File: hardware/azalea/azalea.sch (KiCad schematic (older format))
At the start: 7 parts

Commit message: azalea: completed most of schematic apart from the expansion interface
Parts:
- removed J?: GSG-USB-MICRO-B-SHIELDED, symbol GSG-USB-MICRO-B-SHIELDED
- added C? (x2): 18pF, symbol C
- added C? (x2): 47pF, symbol C
- added C?: 10uF, symbol C
- added C?: 1uF, symbol C
- added C? (x15): 100nF, symbol C
- added D? (x4): LED, symbol LED
- added FB?: FILTER, symbol FILTER
- added J2: GSG-USB-MICRO-B-SHIELDED, symbol GSG-USB-MICRO-B-SHIELDED
- added P?: JTAG, symbol CONN_02X05
- added P?: DBGEN, symbol CONN_01X01
- added P?: TRST, symbol CONN_01X01
- added R? (x12): 10k, symbol R
- added R? (x2): 12.0k, symbol R
- added R? (x2): 33.0, symbol R
- added R? (x4): 330, symbol R
- added SW?: RESET, symbol SW_PUSH
- added SW?: DFU, symbol SW_PUSH
- J1: renamed from J?; Description (none) -> CONN RCPT REV MICRO USB TYPE B; Manufacturer (none) -> FCI; Part Number (none) -> 10103592-0001LF
- U1: renamed from U?; Description (none) -> IC MCU ARM ROMLESS 144LQFP; Manufacturer (none) -> NXP; Part Number (none) -> LPC4330FBD144,551
- U?: Description (none) -> IC REG LDO 3.3V .3A SOT23; Manufacturer (none) -> Diodes Inc.; Part Number (none) -> AP7333-33SAG-7
- U?: Description (none) -> IC USB DUAL ESD PROTECT 6TSOP; Manufacturer (none) -> NXP; Part Number (none) -> IP4220CZ6,125
- U?: value W25Q80BV -> W25Q16DV; Description (none) -> IC FLASH 16MBIT 104MHZ 8SOIC; Manufacturer (none) -> Winbond; Part Number (none) -> W25Q16DVSSIG
- X?: Description (none) -> CRYSTAL 12.000 MHZ 12PF SMD; Manufacturer (none) -> TXC; Part Number (none) -> 7V-12.000MAAE-T
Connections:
- net at U?.1 (IN): now also U1.21 (USB0_VBUS), C?.1, FB?.2
- net VCC: now reaches U?.2 (OUT)
- net VCC: now also U1.107 (VDDIO), U1.111 (VDDIO), U1.131 (VDDREG), U1.141 (VDDIO), U1.16 (USB0_VDDA3V3_DRIVER), U1.17 (USB0_VDDA3V3), U1.25 (VDDREG), U1.36 (VDDIO), U1.41 (VDDIO), U1.5 (VDDIO), U1.59 (VDDREG), U1.71 (VDDIO), U1.77 (VDDIO), U1.94 (VDDREG), U?.8 (VCC), C?.1, C?.1, C?.1, C?.1, C?.1, C?.1, C?.1, C?.1, C?.1, C?.1, C?.1, C?.1, C?.1, C?.1, C?.1, C?.1, P?.1 (P1), R?.1, R?.1, R?.1, R?.1, R?.1, R?.1, R?.1, R?.1, R?.1, R?.1, R?.1, R?.1, SW?.2
- net GND: now reaches U?.3 (GND)
- net GND: now also J1.5 (GND), U1.109 (VSSIO), U1.135 (VSSA), U1.19 (USB0_VSSA_TERM), U1.23 (USB0_VSSA_REF), U1.4 (VSSIO), U1.40 (VSSIO), U1.76 (VSSIO), U?.2 (GND), U?.4 (GND), X?.2, X?.4, C?.2, C?.2, C?.2, C?.2, C?.2, C?.2, C?.2, C?.2, C?.2, C?.2, C?.2, C?.2, C?.2, C?.2, C?.2, C?.2, C?.2, C?.2, C?.2, C?.2, C?.2, J2.5 (GND), P?.3 (P3), P?.5 (P5), P?.9 (P9), R?.1, R?.2, R?.2, R?.2, R?.2, SW?.2
- net at U?.1 (ESD1): now also J1.2 (D-), U1.20 (USB0_DM), U?.6 (ESD4)
- net at U?.3 (ESD2): now also J1.3 (D+), U1.18 (USB0_DP), U?.4 (ESD3)
- net at U?.5 (VP): now also J1.1 (VBUS), FB?.1
- net at J1.4 (ID): now also U1.22 (USB0_ID), R?.2
- net at X?.1: now also U1.12 (XTAL1), C?.1
- net at X?.3: now also U1.13 (XTAL2), C?.1
- net P2_9: now reaches U1.102 (P2_9)
- net P2_9: now also R?.1
- net SPIFI_SCK: now reaches U1.118 (P3_3)
- net SPIFI_SCK: now also U?.6 (CLK)
- net SPIFI_SIO3: now reaches U1.119 (P3_4)
- net SPIFI_SIO3: now also U?.7 (HOLD)
- net SPIFI_SIO2: now reaches U1.121 (P3_5)
- net SPIFI_SIO2: now also U?.3 (WP)
- net SPIFI_MISO: now reaches U1.122 (P3_6)
- net SPIFI_MISO: now also U?.2 (DO)
- net SPIFI_MOSI: now reaches U1.123 (P3_7)
- net SPIFI_MOSI: now also U?.5 (DI)
- net SPIFI_CS: now reaches U1.124 (P3_8)
- net SPIFI_CS: now also U?.1 (CS)
- net WAKEUP: now reaches U1.130 (WAKEUP0)
- net WAKEUP: now also R?.2
- net at U1.24 (USB0_RREF): now also R?.1
- net TDI: now reaches U1.26 (TDI)
- net TDI: now also P?.8 (P8)
- net TCK: now reaches U1.27 (TCK/SWDCLK)
- net TCK: now also P?.4 (P4), R?.2
- net at U1.28 (DBGEN): now also P?.1 (P1), R?.2
- net at U1.29 (TRST): now also P?.1 (P1)
- net TMS: now reaches U1.30 (TMS/SWDIO)
- net TMS: now also P?.2 (P2)
- net TDO: now reaches U1.31 (TDO/SWO)
- net TDO: now also P?.6 (P6), R?.2
- net P1_1: now reaches U1.42 (P1_1)
- net P1_2: now reaches U1.43 (P1_2)
- net P1_2: now also R?.1, R?.2
- net at U1.89 (USB1_DP): now also C?.1, R?.2
- net at U1.90 (USB1_DM): now also C?.1, R?.2
- net at U1.91 (P2_5): now also R?.2, R?.2
- net ISP: now reaches U1.96 (P2_7)
- net ISP: now also R?.2
- net P2_8: now reaches U1.98 (P2_8)
- net P2_8: now also R?.1, SW?.1
- new net: D?.2 (A), R?.2 (x4)
- new net: J2.1 (VBUS), R?.1
- new net: J2.2 (D-), R?.1
- new net: J2.3 (D+), R?.1
- new net LED1: D?.1 (K)
- new net LED2: D?.1 (K)
- new net RESET: P?.10 (P10), R?.2, SW?.1
- new net RXLED: D?.1 (K)
- new net TXLED: D?.1 (K)
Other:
- note added: "TODO\n\nLED control pin selection\nneighbor interface\nUSB1 host mode"
- moved on the sheet: J1, U?, X?

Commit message: azalea: USB1 VBUS switching
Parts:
- added Q?: Q_PMOS_DGS, symbol Q_PMOS_DGS
- added R?: 10k, symbol R
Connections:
- net VBUS: now reaches C?.1, FB?.2, U1.21 (USB0_VBUS), U?.1 (IN)
- net VBUS: now also Q?.3 (S), R?.1
- net at U1.97 (P6_9): now also Q?.2 (G), R?.2
- net at J2.1 (VBUS), R?.1: now also Q?.1 (D)
- no-connect marks 42 -> 41
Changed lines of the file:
@@
 NoConn ~ 11250 6400
 NoConn ~ 11250 6200
-NoConn ~ 11250 4700
 NoConn ~ 11250 4500
 NoConn ~ 11250 4400
@@
 Connection ~ 12750 1650
 Wire Wire Line
-	2800 5100 3050 5100
-Wire Wire Line
-	3050 5100 4500 5100
-Wire Wire Line
-	4500 5100 5100 5100
+	2800 5100 5100 5100
 Wire Wire Line
 	5100 5100 5100 5300
@@
 	5000 5500 5000 5200
 Wire Wire Line
-	5000 5200 4700 5200
-Wire Wire Line
-	4700 5200 2950 5200
-Wire Wire Line
-	2950 5200 2800 5200
+	5000 5200 2800 5200
 Wire Wire Line
 	5750 5800 5850 5800
@@
 	5600 4000 5850 4000
 Wire Wire Line
-	5650 5100 5750 5100
-Wire Wire Line
-	5750 5100 5850 5100
+	5650 5100 5850 5100
 Wire Wire Line
 	5850 5200 5750 5200
@@
 Connection ~ 2950 5200
 Wire Wire Line
-	2800 5300 3150 5300
-Wire Wire Line
-	3150 5300 3500 5300
+	2800 5300 3500 5300
 Wire Wire Line
 	3500 5300 3500 5450
@@
 	4300 5450 4900 5450
 Wire Wire Line
-	4900 5450 4900 5600
-Wire Wire Line
-	4900 5600 4900 6850
+	4900 5450 4900 6850
 Wire Wire Line
 	3700 6850 3700 6950
@@
 	4800 5700 4800 5000
 Wire Wire Line
-	4800 5000 3400 5000
-Wire Wire Line
-	3400 5000 2800 5000
+	4800 5000 2800 5000
 Wire Wire Line
 	2800 4900 2900 4900
@@
 	5250 4800 5250 4150
 Wire Wire Line
-	5250 4150 5000 4150
-Wire Wire Line
-	5000 4150 4900 4150
+	5250 4150 4900 4150
 Wire Wire Line
 	5850 4700 5350 4700
@@
 	5350 3900 4200 3900
 Wire Wire Line
-	4200 3900 4200 4150
-Wire Wire Line
-	4200 4150 4200 4350
+	4200 3900 4200 4350
 Wire Wire Line
 	4200 4150 4300 4150
@@
 	3350 6750 3450 6750
 Wire Wire Line
-	3450 6650 3450 6750
-Wire Wire Line
-	3450 6750 3450 6950
+	3450 6650 3450 6950
 Connection ~ 3450 6750
 Wire Wire Line
-	4900 6850 3700 6850
-Wire Wire Line
-	3700 6850 3350 6850
+	4900 6850 3350 6850
 Connection ~ 3700 6850
 Wire Wire Line
@@
 	12750 1650 12300 1650
 Wire Wire Line
-	12750 1550 12750 1650
-Wire Wire Line
-	12750 1650 12750 1750
+	12750 1550 12750 1750
 Wire Wire Line
 	12200 8100 12200 8200
 Wire Wire Line
-	12200 8200 12300 8200
-Wire Wire Line
-	12300 8200 12600 8200
-Wire Wire Line
-	12600 8200 12900 8200
-Wire Wire Line
-	12900 8200 13200 8200
-Wire Wire Line
-	13200 8200 13500 8200
-Wire Wire Line
-	13500 8200 13800 8200
-Wire Wire Line
-	13800 8200 14100 8200
-Wire Wire Line
-	14100 8200 14400 8200
-Wire Wire Line
-	14400 8200 14700 8200
-Wire Wire Line
-	14700 8200 15000 8200
-Wire Wire Line
-	15000 8200 15300 8200
-Wire Wire Line
-	15300 8200 15600 8200
-Wire Wire Line
-	15600 8200 15900 8200
-Wire Wire Line
-	15900 8200 16200 8200
+	12200 8200 16200 8200
 Wire Wire Line
 	16200 8200 16200 8300
@@
 	16200 8700 16200 8600
 Wire Wire Line
-	12200 8700 12300 8700
-Wire Wire Line
-	12300 8700 12600 8700
-Wire Wire Line
-	12600 8700 12900 8700
-Wire Wire Line
-	12900 8700 13200 8700
-Wire Wire Line
-	13200 8700 13500 8700
-Wire Wire Line
-	13500 8700 13800 8700
-Wire Wire Line
-	13800 8700 14100 8700
-Wire Wire Line
-	14100 8700 14400 8700
-Wire Wire Line
-	14400 8700 14700 8700
-Wire Wire Line
-	14700 8700 15000 8700
-Wire Wire Line
-	15000 8700 15300 8700
-Wire Wire Line
-	15300 8700 15600 8700
-Wire Wire Line
-	15600 8700 15900 8700
-Wire Wire Line
-	15900 8700 16200 8700
+	12200 8700 16200 8700
 Wire Wire Line
 	12200 8700 12200 8800
@@
 	5000 8900 4300 8900
 Wire Wire Line
-	4300 8700 4650 8700
-Wire Wire Line
-	4650 8700 5100 8700
+	4300 8700 5100 8700
 Wire Wire Line
 	5100 8700 5100 6200
@@
 	5500 6600 5500 8800
 Wire Wire Line
-	5500 8800 4850 8800
-Wire Wire Line
-	4850 8800 4300 8800
+	5500 8800 4300 8800
 Wire Wire Line
 	4500 9000 4300 9000
@@
 	5200 6300 5200 8000
 Wire Wire Line
-	5200 8000 4450 8000
-Wire Wire Line
-	4450 8000 4250 8000
+	5200 8000 4250 8000
 $Comp
 L R R?
@@
 $EndComp
 Wire Wire Line
-	3700 8700 3700 8800
-Wire Wire Line
-	3700 8800 3700 9000
-Wire Wire Line
-	3700 9000 3700 9100
+	3700 8700 3700 9100
 Wire Wire Line
 	3700 8700 3800 8700
@@
 $EndComp
 Wire Wire Line
-	8200 2050 8200 2150
-Wire Wire Line
-	8200 2150 8200 2650
+	8200 2050 8200 2650
 Wire Wire Line
 	7950 2150 8200 2150
@@
 $EndComp
 Wire Wire Line
-	11250 4800 11950 4800
-Wire Wire Line
-	11950 4800 12150 4800
+	11250 4800 12150 4800
 Wire Wire Line
 	11950 4800 11950 4700
@@
 $EndComp
 Wire Wire Line
-	1050 1450 1300 1450
-Wire Wire Line
-	1300 1450 1400 1450
+	1050 1450 1400 1450
 Wire Wire Line
 	1300 1350 1300 1450
@@
 $EndComp
 Wire Wire Line
-	2350 1450 2600 1450
-Wire Wire Line
-	2600 1450 2700 1450
+	2350 1450 2700 1450
 Connection ~ 2600 1450
 $Comp
@@
 	13450 4200 13200 4200
 Wire Wire Line
-	13200 4200 13200 4300
-Wire Wire Line
-	13200 4600 13200 4700
-Wire Wire Line
-	13200 4700 13200 4800
+	13200 4100 13200 4300
+Wire Wire Line
+	13200 4600 13200 4800
 Wire Wire Line
 	13200 4700 12850 4700
@@
 	13550 5500 13200 5500
 Wire Wire Line
-	11250 5500 12500 5500
-Wire Wire Line
-	12500 5500 12900 5500
+	11250 5500 12900 5500
 Wire Wire Line
 	13550 5400 12900 5400
 Wire Wire Line
-	11250 5400 12150 5400
-Wire Wire Line
-	12150 5400 12600 5400
+	11250 5400 12600 5400
 $Comp
 L R R?
@@
 Text Label 1450 3900 1    40   ~ 0
 LED2
+$Comp
+L Q_PMOS_DGS Q?
+U 1 1 55EA7DFE
+P 13100 3900
+F 0 "Q?" H 13400 3950 50  0000 R CNN
+F 1 "Q_PMOS_DGS" H 13750 3850 50  0000 R CNN
+F 2 "" H 13300 4000 29  0000 C CNN
+F 3 "" H 13100 3900 60  0000 C CNN
+	1    13100 3900
+	1    0    0    1
+$EndComp
+Text Label 3950 6850 0    40   ~ 0
+VBUS
+Connection ~ 13200 4200
+Wire Wire Line
+	13200 3400 13200 3700
+Text Label 13200 3400 3    40   ~ 0
+VBUS
+$Comp
+L R R?
+U 1 1 55EA933A
+P 12950 3600
+F 0 "R?" V 13030 3600 50  0000 C CNN
+F 1 "10k" V 12950 3600 50  0000 C CNN
+F 2 "" V 12880 3600 30  0000 C CNN
+F 3 "" H 12950 3600 30  0000 C CNN
+F 4 "Panasonic" H 12950 3600 60  0001 C CNN "Manufacturer"
+F 5 "ERJ-3GEYJ103V" H 12950 3600 60  0001 C CNN "Part Number"
+F 6 "RES 10K OHM 1/10W 5% 0603 SMD" H 12950 3600 60  0001 C CNN "Description"
+	1    12950 3600
+	0    1    1    0
+$EndComp
+Wire Wire Line
+	13100 3600 13200 3600
+Connection ~ 13200 3600
+Wire Wire Line
+	12800 3600 12700 3600
+Wire Wire Line
+	12700 3600 12700 3900
+Wire Wire Line
+	11750 3900 12900 3900
+Wire Wire Line
+	11250 4700 11750 4700
+Wire Wire Line
+	11750 4700 11750 3900
+Connection ~ 12700 3900
 $EndSCHEMATC

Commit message: azalea: I2C pull-ups, optional RTC section
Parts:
- added C? (x2): 18pF, symbol C
- added P? (x2): CONN_02X20, symbol CONN_02X20
- added P?: CONN_02X03, symbol CONN_02X03
- added R? (x2): 1.8k, symbol R
- added X?: RTC_XTAL, symbol Crystal
- P? (x3): Note (none) -> DNP
- gave numbers to parts that had none: 1
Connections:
- net GND: now also C?.2, C?.2, P?.1 (P1), P?.1 (P1), P?.3 (P3), P?.9 (P9)
- net MISO: now also P?.1 (P1)
- net MOSI: now also P?.3 (P3)
- net RESET: now also U1.128 (RESET), P?.4 (P4)
- net SCK: now also P?.7 (P7)
- net SSEL: now also P?.5 (P5)
- net VBUS: now also P?.3 (P3)
- net VCC: now also U1.137 (VDDA), P?.2 (P2), P?.2 (P2), P?.4 (P4), R?.1, R?.1
- net RTCX1: now reaches U1.125 (RTCX1)
- net RTCX1: now also C?.1, X?.1
- net RTCX2: now reaches U1.126 (RTCX2)
- net RTCX2: now also C?.1, X?.2
- net VBAT: now reaches U1.127 (VBAT)
- net VBAT: now also P?.2 (P2)
- net RTC_ALARM: now reaches U1.129 (RTC_ALARM)
- net RTC_ALARM: now also P?.6 (P6)
- net I2C0_SCL: now reaches U1.92 (I2C0_SCL)
- net I2C0_SCL: now also R?.2
- net I2C0_SDA: now reaches U1.93 (I2C0_SDA)
- net I2C0_SDA: now also R?.2
- net RXLED renamed LED3
- net TXLED renamed LED4
- net WAKEUP renamed WAKEUP0
- net WAKEUP0: now also P?.5 (P5)
- no-connect marks 41 -> 37
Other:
- note added: "TODO\n\nLED control pin selection\nneighbor interface\nPMOS pinout"
- note removed: "TODO\n\nLED control pin selection\nneighbor interface\nUSB1 host mode"
- moved on the sheet: P?

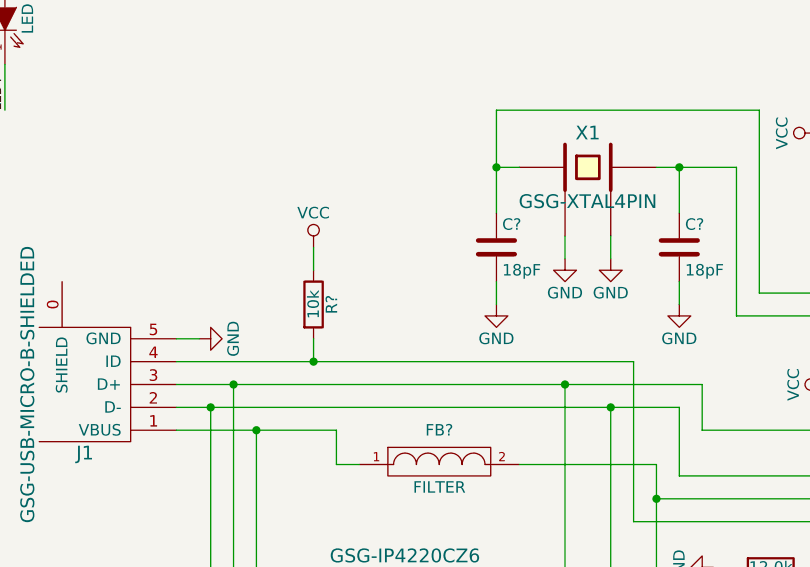
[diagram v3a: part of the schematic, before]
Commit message: azalea: removed USB0_ID pull-up as there is an internal pull-up
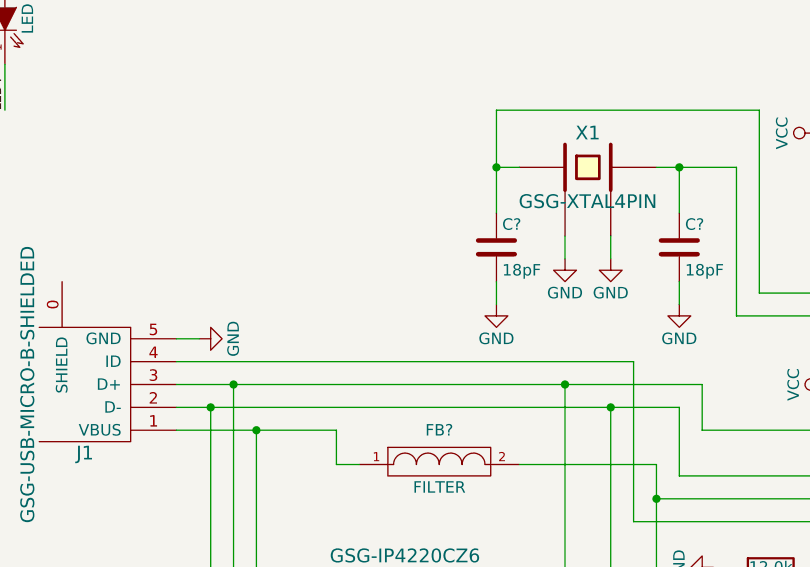
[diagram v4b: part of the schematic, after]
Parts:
- removed R?: 10k, symbol R
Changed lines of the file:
@@
-$EndComp
-$Comp
-L R R?
-U 1 1 55E3D710
-P 3400 4750
-F 0 "R?" V 3480 4750 50  0000 C CNN
-F 1 "10k" V 3400 4750 50  0000 C CNN
-F 2 "" V 3330 4750 30  0000 C CNN
-F 3 "" H 3400 4750 30  0000 C CNN
-F 4 "Panasonic" H 3400 4750 60  0001 C CNN "Manufacturer"
-F 5 "ERJ-3GEYJ103V" H 3400 4750 60  0001 C CNN "Part Number"
-F 6 "RES 10K OHM 1/10W 5% 0603 SMD" H 3400 4750 60  0001 C CNN "Description"
-	1    3400 4750
-	1    0    0    -1
 $EndComp
 $Comp
@@
 	1    2900 4900
 	0    -1   -1   0
-$EndComp
-$Comp
-L VCC #PWR?
-U 1 1 55E3D935
-P 3400 4500
-F 0 "#PWR?" H 3400 4350 50  0001 C CNN
-F 1 "VCC" H 3400 4650 50  0000 C CNN
-F 2 "" H 3400 4500 60  0000 C CNN
-F 3 "" H 3400 4500 60  0000 C CNN
-	1    3400 4500
-	1    0    0    -1
 $EndComp
 $Comp
@@
 	4800 5000 4800 5700
 Wire Wire Line
-	2800 5000 3400 5000
-Wire Wire Line
-	3400 5000 4800 5000
+	2800 5000 4800 5000
 Wire Wire Line
 	2800 4900 2900 4900
 Wire Wire Line
-	3400 4500 3400 4600
-Wire Wire Line
-	3400 4900 3400 5000
-Connection ~ 3400 5000
-Wire Wire Line
 	5850 4800 5250 4800

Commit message: azalea: proper USB1 switching
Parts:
- removed Q?: Q_PMOS_DGS, symbol Q_PMOS_DGS
- added C?: 1uF, symbol C
- added C?: 10uF, symbol C
- added R?: 49.9k, symbol R
- added R?: 10k, symbol R
- added U?: NX5P2553GV, symbol NX5P2553GV
- J1, J2: value GSG-USB-MICRO-B-SHIELDED -> USB-MICRO-B-SHIELDED; symbol GSG-USB-MICRO-B-SHIELDED -> USB-MICRO-B-SHIELDED
- U?: value GSG-IP4220CZ6 -> IP4220CZ6; symbol GSG-IP4220CZ6 -> IP4220CZ6
- X1: value GSG-XTAL4PIN -> XTAL4PIN; symbol GSG-XTAL4PIN -> XTAL4PIN
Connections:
- net GND: now also R?.1, C?.2, C?.2, R?.1, U?.2 (GND)
- net VBUS: now also C?.1, U?.1 (VIN); no longer R?.1
- net VCC: now also R?.2
- net at U1.100 (P6_10): now also R?.1, U?.4 (FAULT)
- net at R?.2, U1.97 (P6_9): now also U?.3 (EN)
- net at J2.1 (VBUS), R?.1: now also C?.1, U?.6 (VOUT)
- new net: R?.2, U?.5 (ILIM)
- no-connect marks 37 -> 36
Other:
- note added: "TODO\n\nLED control pin selection\nneighbor interface"
- note removed: "TODO\n\nLED control pin selection\nneighbor interface\nPMOS pinout"
- moved on the sheet: R?

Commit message: azalea: pin selections
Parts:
- D?: value LED -> LED1
- D?: value LED -> LED2
- D?: value LED -> LED3
- D?: value LED -> LED4
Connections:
- net LED1: now also U1.132 (P7_4)
- net LED2: now also U1.133 (P7_5)
- net LED3: now also U1.134 (P7_6)
- net LED4: now also U1.3 (P4_1)
- net P1_1: now also R?.2
- net P1_2: no longer R?.2
- net USB1_FAULT: now reaches R?.1, U?.4 (FAULT)
- net USB1_FAULT: now also U1.117 (P7_3); no longer U1.100 (P6_10)
- net at U1.101 (P6_11): now also R?.2, R?.2
- net at U1.103 (P6_12): now also R?.2, U?.3 (EN)
- now unconnected: U1.91 (P2_5), U1.97 (P6_9)
- no-connect marks 36 -> 19
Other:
- note added: "TODO\n\nneighbor interface"
- note removed: "TODO\n\nLED control pin selection\nneighbor interface"
